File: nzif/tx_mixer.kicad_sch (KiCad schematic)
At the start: 28 parts, among them U801 SN74CBT3125CPW, U802 SN74CBT3125CPW, U803 SN74CBT3125CPW, U804 SN74CBT3125CPW

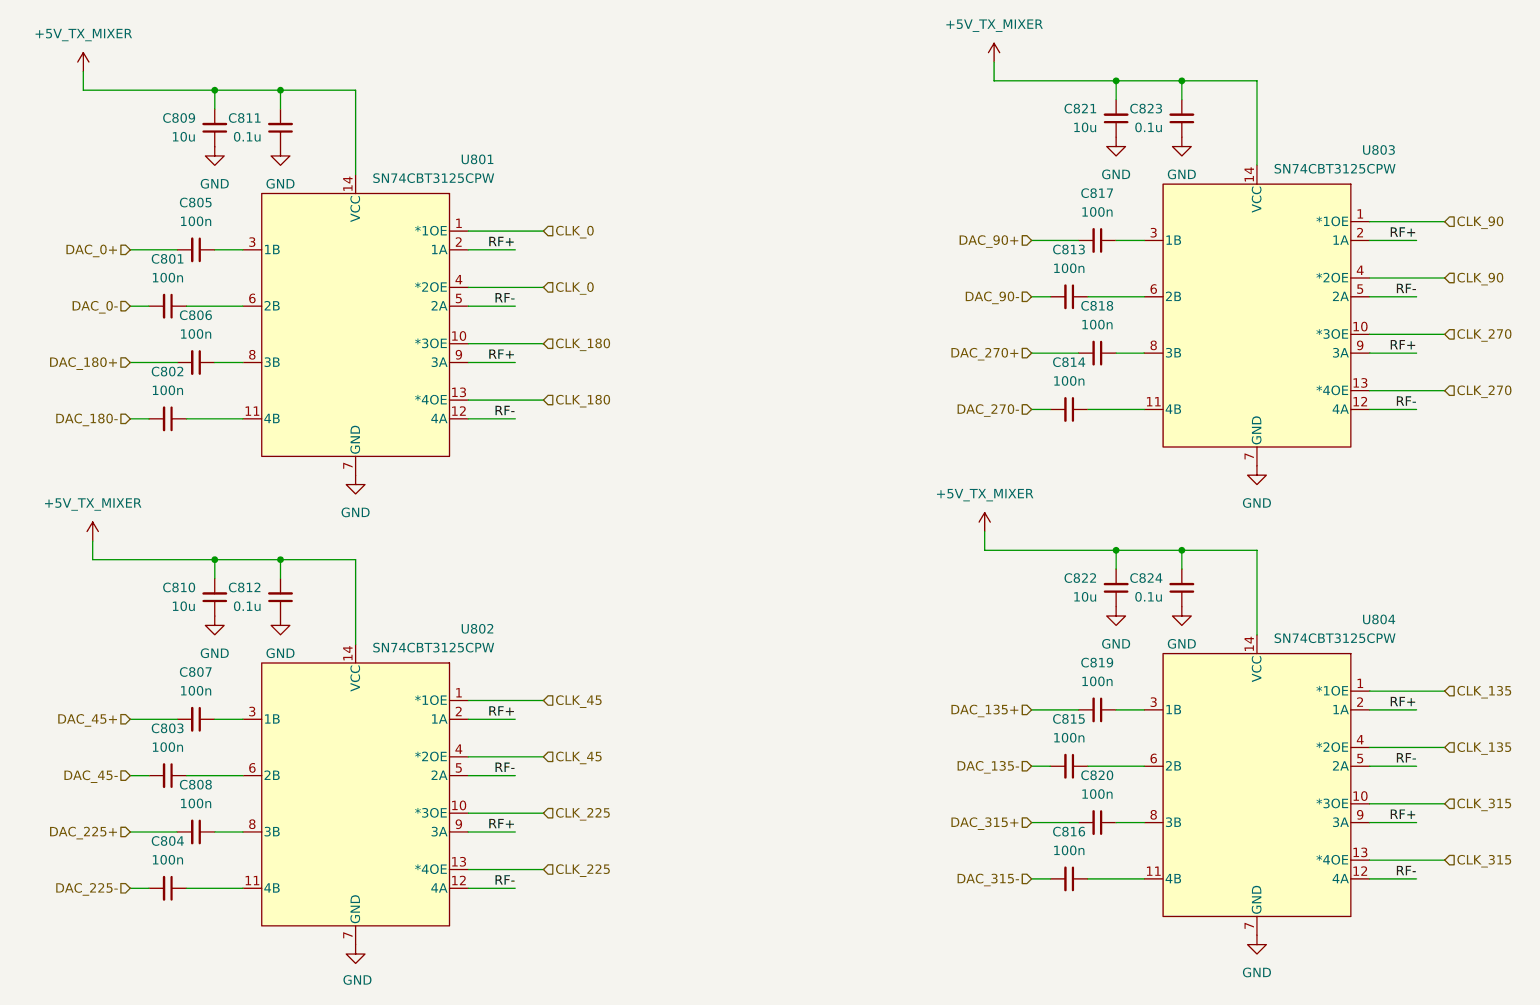
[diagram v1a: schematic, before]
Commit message: top sheet wiring
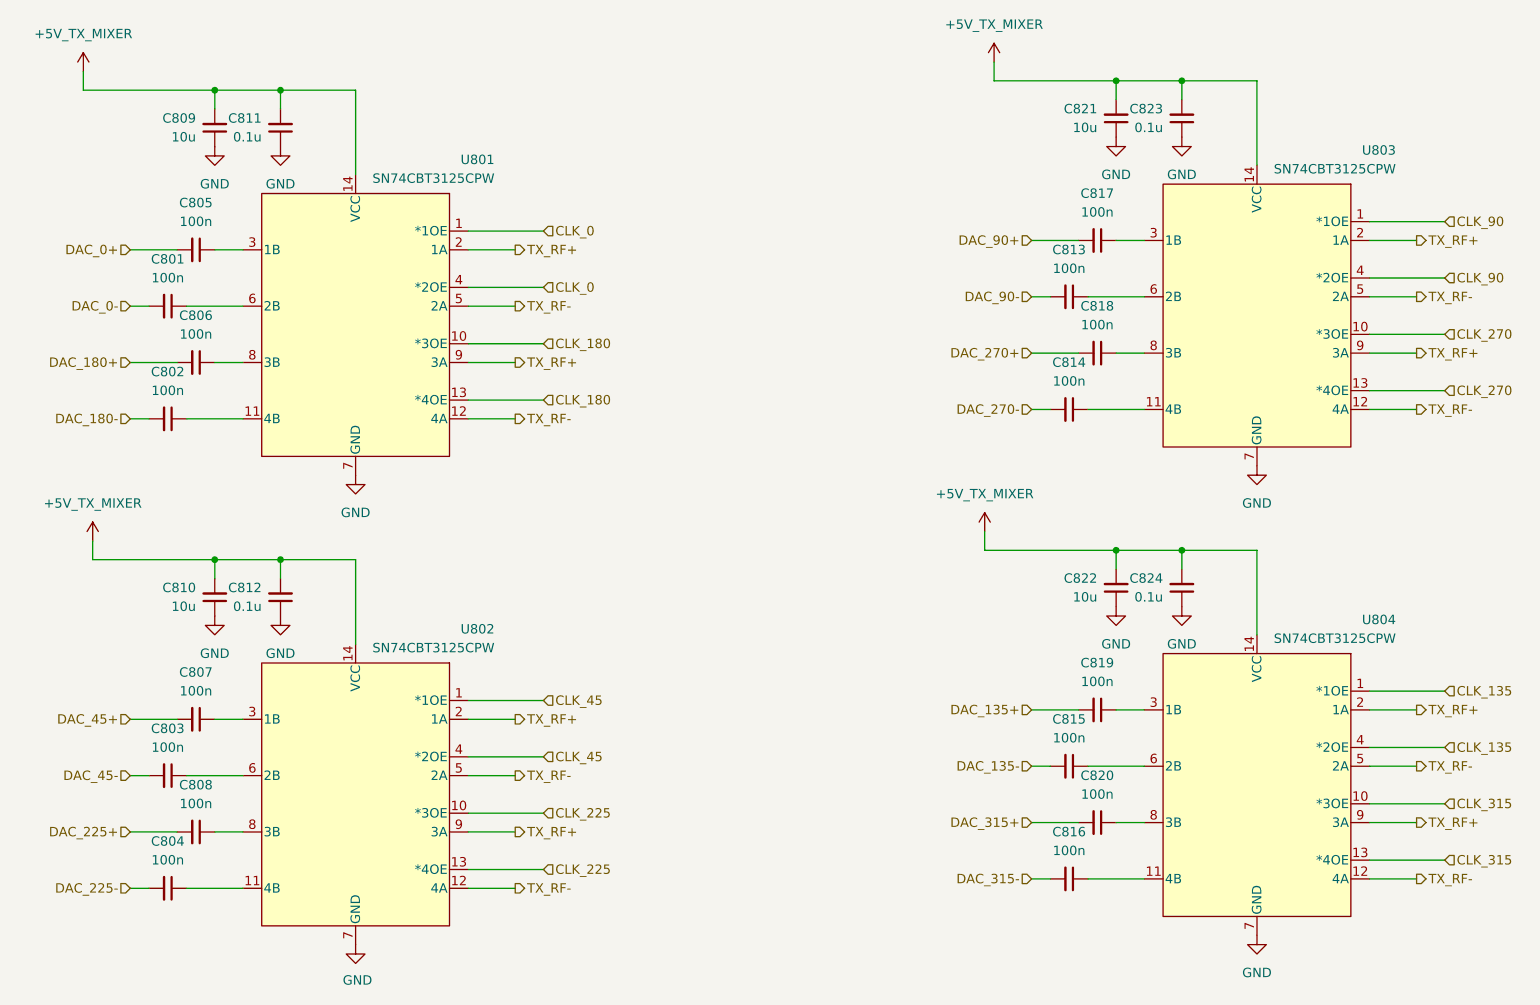
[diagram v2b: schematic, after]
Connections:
- net RF+ renamed TX_RF+
- net RF- renamed TX_RF-
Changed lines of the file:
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@@
 		)
 	)
-	(label "RF+"
-		(at 138.43 71.12 180)
-		(effects
-			(font
-				(size 1.27 1.27)
-			)
-			(justify right bottom)
-		)
-	)
-	(label "RF+"
-		(at 260.35 118.11 180)
-		(effects
-			(font
-				(size 1.27 1.27)
-			)
-			(justify right bottom)
-		)
-	)
-	(label "RF+"
-		(at 260.35 69.85 180)
-		(effects
-			(font
-				(size 1.27 1.27)
-			)
-			(justify right bottom)
-		)
-	)
-	(label "RF-"
-		(at 138.43 78.74 180)
-		(effects
-			(font
-				(size 1.27 1.27)
-			)
-			(justify right bottom)
-		)
-	)
-	(label "RF-"
-		(at 260.35 140.97 180)
-		(effects
-			(font
-				(size 1.27 1.27)
-			)
-			(justify right bottom)
-		)
-	)
-	(label "RF-"
-		(at 138.43 63.5 180)
-		(effects
-			(font
-				(size 1.27 1.27)
-			)
-			(justify right bottom)
-		)
-	)
-	(label "RF+"
-		(at 138.43 134.62 180)
-		(effects
-			(font
-				(size 1.27 1.27)
-			)
-			(justify right bottom)
-		)
-	)
-	(label "RF-"
-		(at 260.35 125.73 180)
-		(effects
-			(font
-				(size 1.27 1.27)
-			)
-			(justify right bottom)
-		)
-	)
-	(label "RF-"
-		(at 138.43 127 180)
-		(effects
-			(font
-				(size 1.27 1.27)
-			)
-			(justify right bottom)
-		)
-	)
-	(label "RF+"
-		(at 138.43 55.88 180)
-		(effects
-			(font
-				(size 1.27 1.27)
-			)
-			(justify right bottom)
-		)
-	)
-	(label "RF-"
-		(at 260.35 77.47 180)
-		(effects
-			(font
-				(size 1.27 1.27)
-			)
-			(justify right bottom)
-		)
-	)
-	(label "RF-"
-		(at 138.43 142.24 180)
-		(effects
-			(font
-				(size 1.27 1.27)
-			)
-			(justify right bottom)
-		)
-	)
-	(label "RF-"
-		(at 260.35 62.23 180)
-		(effects
-			(font
-				(size 1.27 1.27)
-			)
-			(justify right bottom)
-		)
-	)
-	(label "RF+"
-		(at 260.35 133.35 180)
-		(effects
-			(font
-				(size 1.27 1.27)
-			)
-			(justify right bottom)
-		)
-	)
-	(label "RF+"
-		(at 138.43 119.38 180)
-		(effects
-			(font
-				(size 1.27 1.27)
-			)
-			(justify right bottom)
-		)
-	)
-	(label "RF+"
-		(at 260.35 54.61 180)
-		(effects
-			(font
-				(size 1.27 1.27)
-			)
-			(justify right bottom)
+	(hierarchical_label "TX_RF-"
+		(shape output)
+		(at 138.43 127 0)
+		(effects
+			(font
+				(size 1.27 1.27)
+			)
+			(justify left)
+		)
+	)
+	(hierarchical_label "TX_RF+"
+		(shape output)
+		(at 260.35 118.11 0)
+		(effects
+			(font
+				(size 1.27 1.27)
+			)
+			(justify left)
 		)
 	)
@@
 		)
 	)
+	(hierarchical_label "TX_RF+"
+		(shape output)
+		(at 260.35 69.85 0)
+		(effects
+			(font
+				(size 1.27 1.27)
+			)
+			(justify left)
+		)
+	)
+	(hierarchical_label "TX_RF-"
+		(shape output)
+		(at 138.43 142.24 0)
+		(effects
+			(font
+				(size 1.27 1.27)
+			)
+			(justify left)
+		)
+	)
 	(hierarchical_label "DAC_45+"
 		(shape input)
@@
 		)
 	)
+	(hierarchical_label "TX_RF+"
+		(shape output)
+		(at 260.35 54.61 0)
+		(effects
+			(font
+				(size 1.27 1.27)
+			)
+			(justify left)
+		)
+	)
 	(hierarchical_label "DAC_315+"
 		(shape input)
@@
 		)
 	)
+	(hierarchical_label "TX_RF-"
+		(shape output)
+		(at 260.35 77.47 0)
+		(effects
+			(font
+				(size 1.27 1.27)
+			)
+			(justify left)
+		)
+	)
 	(hierarchical_label "CLK_225"
 		(shape input)
@@
 		)
 	)
+	(hierarchical_label "TX_RF+"
+		(shape output)
+		(at 138.43 134.62 0)
+		(effects
+			(font
+				(size 1.27 1.27)
+			)
+			(justify left)
+		)
+	)
 	(hierarchical_label "CLK_90"
 		(shape input)
@@
 		)
 	)
+	(hierarchical_label "TX_RF+"
+		(shape output)
+		(at 138.43 71.12 0)
+		(effects
+			(font
+				(size 1.27 1.27)
+			)
+			(justify left)
+		)
+	)
 	(hierarchical_label "CLK_135"
 		(shape input)
@@
 		)
 	)
+	(hierarchical_label "TX_RF-"
+		(shape output)
+		(at 138.43 78.74 0)
+		(effects
+			(font
+				(size 1.27 1.27)
+			)
+			(justify left)
+		)
+	)
 	(hierarchical_label "CLK_0"
 		(shape input)
@@
 		)
 	)
+	(hierarchical_label "TX_RF-"
+		(shape output)
+		(at 260.35 62.23 0)
+		(effects
+			(font
+				(size 1.27 1.27)
+			)
+			(justify left)
+		)
+	)
 	(hierarchical_label "CLK_270"
 		(shape input)
@@
 		)
 	)
+	(hierarchical_label "TX_RF+"
+		(shape output)
+		(at 138.43 55.88 0)
+		(effects
+			(font
+				(size 1.27 1.27)
+			)
+			(justify left)
+		)
+	)
+	(hierarchical_label "TX_RF+"
+		(shape output)
+		(at 138.43 119.38 0)
+		(effects
+			(font
+				(size 1.27 1.27)
+			)
+			(justify left)
+		)
+	)
+	(hierarchical_label "TX_RF-"
+		(shape output)
+		(at 138.43 63.5 0)
+		(effects
+			(font
+				(size 1.27 1.27)
+			)
+			(justify left)
+		)
+	)
 	(hierarchical_label "CLK_135"
 		(shape input)
@@
 		)
 	)
+	(hierarchical_label "TX_RF+"
+		(shape output)
+		(at 260.35 133.35 0)
+		(effects
+			(font
+				(size 1.27 1.27)
+			)
+			(justify left)
+		)
+	)
 	(hierarchical_label "DAC_225-"
 		(shape input)
@@
 		)
 	)
+	(hierarchical_label "TX_RF-"
+		(shape output)
+		(at 260.35 125.73 0)
+		(effects
+			(font
+				(size 1.27 1.27)
+			)
+			(justify left)
+		)
+	)
 	(hierarchical_label "DAC_180+"
 		(shape input)
@@
 		)
 	)
+	(hierarchical_label "TX_RF-"
+		(shape output)
+		(at 260.35 140.97 0)
+		(effects
+			(font
+				(size 1.27 1.27)
+			)
+			(justify left)
+		)
+	)

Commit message: updates to top level
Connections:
- net +5V_TX_MIXER renamed +3.3V_TX_MIXER
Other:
- note added: "Make sure these are the 3.3V version of the switches. Tx needs 3.3V, Rx needs 5V"
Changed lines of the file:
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@@
 		(company "Andy McCann KA3KAF and Doug McCann KA3KAG")
 	)
+	(text "Make sure these are the 3.3V version of the switches.  \nTx needs 3.3V, Rx needs 5V"
+		(exclude_from_sim no)
+		(at 163.83 96.012 0)
+		(effects
+			(font
+				(size 1.27 1.27)
+			)
+		)
+	)
 	(junction
 		(at 97.79 97.79)
@@
 			)
 		)
-		(property "Value" "+5V_TX_MIXER"
+		(property "Value" "+3.3V_TX_MIXER"
 			(at 81.28 90.17 0)
 			(show_name no)
@@
 			)
 		)
-		(property "Value" "+5V_TX_MIXER"
+		(property "Value" "+3.3V_TX_MIXER"
 			(at 80.01 26.67 0)
 			(show_name no)
@@
 			)
 		)
-		(property "Value" "+5V_TX_MIXER"
+		(property "Value" "+3.3V_TX_MIXER"
 			(at 201.93 88.9 0)
 			(show_name no)
@@
 			)
 		)
-		(property "Value" "+5V_TX_MIXER"
+		(property "Value" "+3.3V_TX_MIXER"
 			(at 203.2 25.4 0)
 			(show_name no)

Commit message: added datasheets
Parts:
- U801, U802, U803, U804: value SN74CBT3125CPW -> SN74CBTLV3125
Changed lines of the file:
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@@
 			)
 		)
-		(property "Value" "SN74CBT3125CPW"
+		(property "Value" "SN74CBTLV3125"
 			(at 257.556 44.958 0)
 			(show_name no)
@@
 			)
 		)
-		(property "Datasheet" "https://www.ti.com/lit/gpn/sn74cbt3125c"
+		(property "Datasheet" "https://www.ti.com/lit/ds/symlink/sn74cbtlv3125.pdf?ts=1775846396408"
 			(at 236.22 64.77 0)
 			(hide yes)
@@
 			)
 		)
-		(property "Value" "SN74CBT3125CPW"
+		(property "Value" "SN74CBTLV3125"
 			(at 135.636 46.228 0)
 			(show_name no)
@@
 			)
 		)
-		(property "Datasheet" "https://www.ti.com/lit/gpn/sn74cbt3125c"
+		(property "Datasheet" "https://www.ti.com/lit/ds/symlink/sn74cbtlv3125.pdf?ts=1775846396408"
 			(at 114.3 66.04 0)
 			(hide yes)
@@
 			)
 		)
-		(property "Value" "SN74CBT3125CPW"
+		(property "Value" "SN74CBTLV3125"
 			(at 257.556 108.458 0)
 			(show_name no)
@@
 			)
 		)
-		(property "Datasheet" "https://www.ti.com/lit/gpn/sn74cbt3125c"
+		(property "Datasheet" "https://www.ti.com/lit/ds/symlink/sn74cbtlv3125.pdf?ts=1775846396408"
 			(at 236.22 128.27 0)
 			(hide yes)
@@
 			)
 		)
-		(property "Value" "SN74CBT3125CPW"
+		(property "Value" "SN74CBTLV3125"
 			(at 135.636 109.728 0)
 			(show_name no)
@@
 			)
 		)
-		(property "Datasheet" "https://www.ti.com/lit/gpn/sn74cbt3125c"
+		(property "Datasheet" "https://www.ti.com/lit/ds/symlink/sn74cbtlv3125.pdf?ts=1775846396408"
 			(at 114.3 129.54 0)
 			(hide yes)

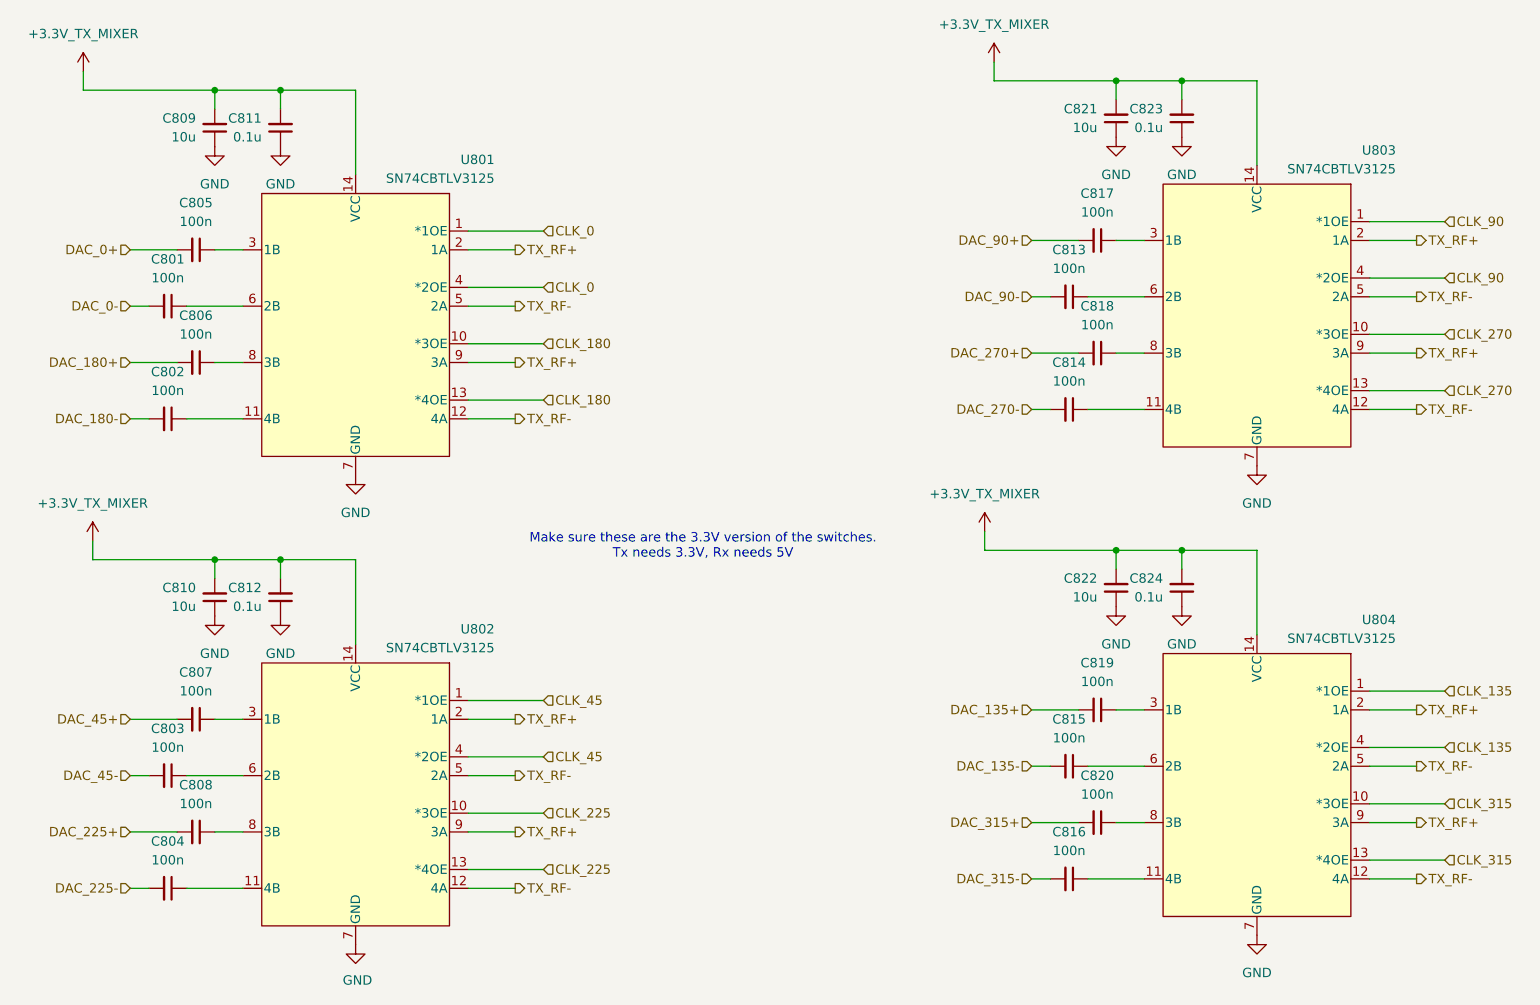
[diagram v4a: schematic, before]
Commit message: Fix ERC errors: symbol pin types and schematic corrections
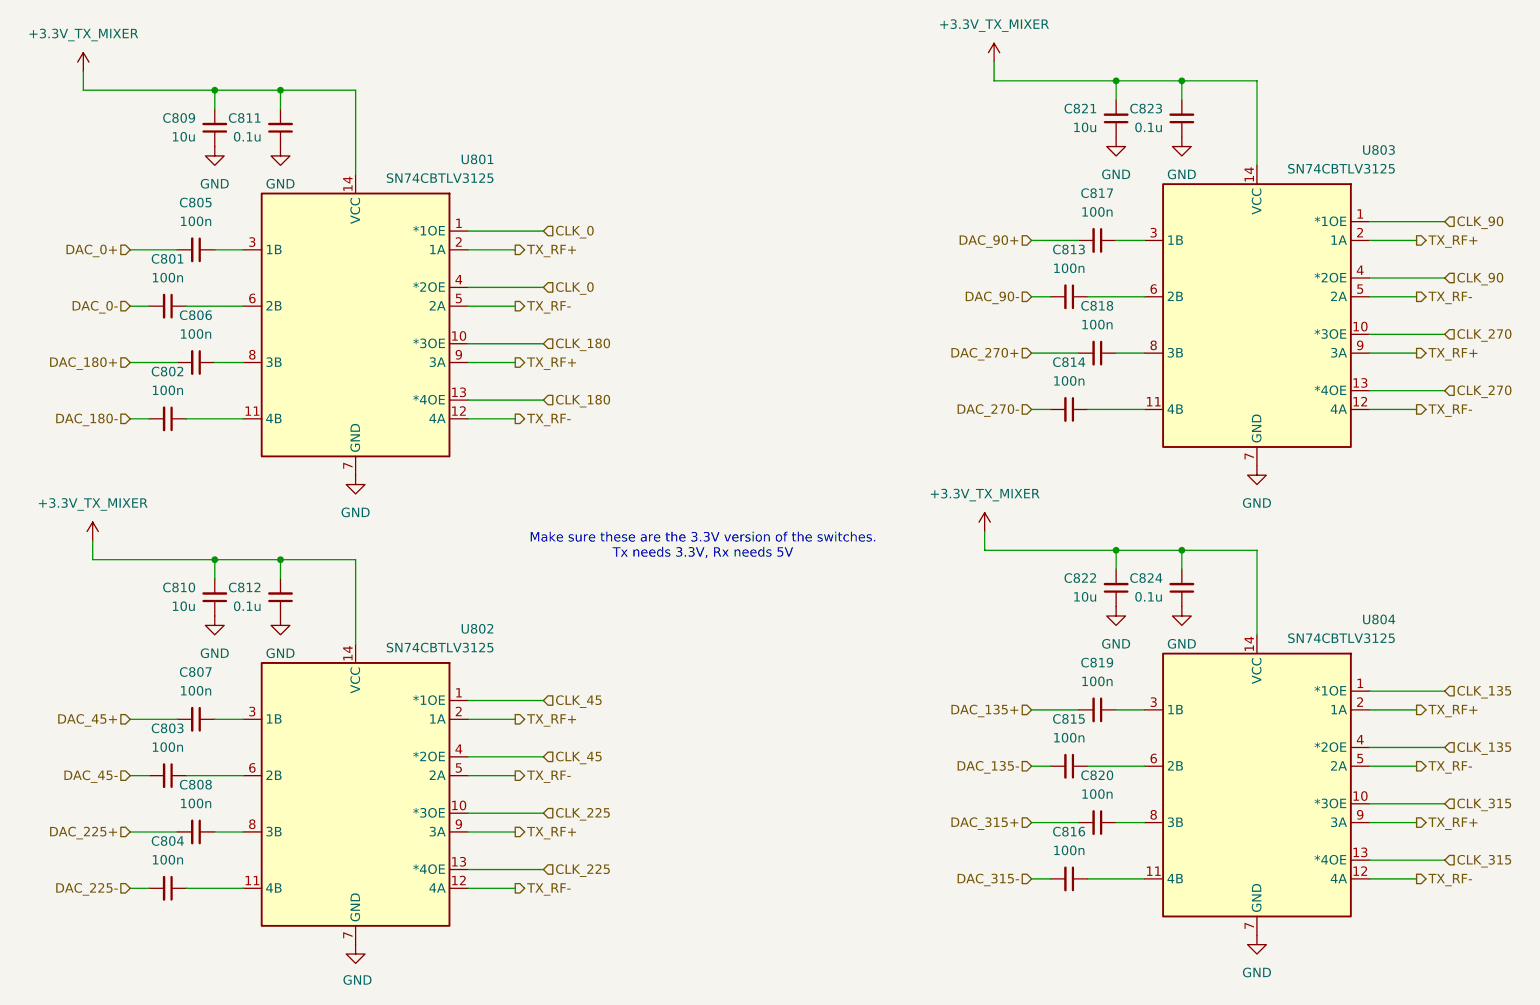
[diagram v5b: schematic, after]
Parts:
- U801, U802, U803, U804: footprint nzif_footprints:PW14 -> Package_SO:TSSOP-14-1EP_4.4x5mm_P0.65mm
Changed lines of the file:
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@@
 			)
 		)
-		(property "Footprint" "nzif_footprints:PW14"
+		(property "Footprint" "Package_SO:TSSOP-14-1EP_4.4x5mm_P0.65mm"
 			(at 287.02 39.37 0)
 			(hide yes)
@@
 			)
 		)
-		(property "Datasheet" "https://www.ti.com/lit/ds/symlink/sn74cbtlv3125.pdf?ts=1775846396408"
+		(property "Datasheet" "https://www.ti.com/lit/gpn/sn74cbt3125c"
 			(at 236.22 64.77 0)
 			(hide yes)
@@
 			)
 		)
-		(property "Footprint" "nzif_footprints:PW14"
+		(property "Footprint" "Package_SO:TSSOP-14-1EP_4.4x5mm_P0.65mm"
 			(at 165.1 40.64 0)
 			(hide yes)
@@
 			)
 		)
-		(property "Datasheet" "https://www.ti.com/lit/ds/symlink/sn74cbtlv3125.pdf?ts=1775846396408"
+		(property "Datasheet" "https://www.ti.com/lit/gpn/sn74cbt3125c"
 			(at 114.3 66.04 0)
 			(hide yes)
@@
 			)
 		)
-		(property "Footprint" "nzif_footprints:PW14"
+		(property "Footprint" "Package_SO:TSSOP-14-1EP_4.4x5mm_P0.65mm"
 			(at 287.02 102.87 0)
 			(hide yes)
@@
 			)
 		)
-		(property "Datasheet" "https://www.ti.com/lit/ds/symlink/sn74cbtlv3125.pdf?ts=1775846396408"
+		(property "Datasheet" "https://www.ti.com/lit/gpn/sn74cbt3125c"
 			(at 236.22 128.27 0)
 			(hide yes)
@@
 			)
 		)
-		(property "Footprint" "nzif_footprints:PW14"
+		(property "Footprint" "Package_SO:TSSOP-14-1EP_4.4x5mm_P0.65mm"
 			(at 165.1 104.14 0)
 			(hide yes)
@@
 			)
 		)
-		(property "Datasheet" "https://www.ti.com/lit/ds/symlink/sn74cbtlv3125.pdf?ts=1775846396408"
+		(property "Datasheet" "https://www.ti.com/lit/gpn/sn74cbt3125c"
 			(at 114.3 129.54 0)
 			(hide yes)
